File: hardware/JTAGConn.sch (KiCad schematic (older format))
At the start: 5 parts, among them CON1 FPC_6POS

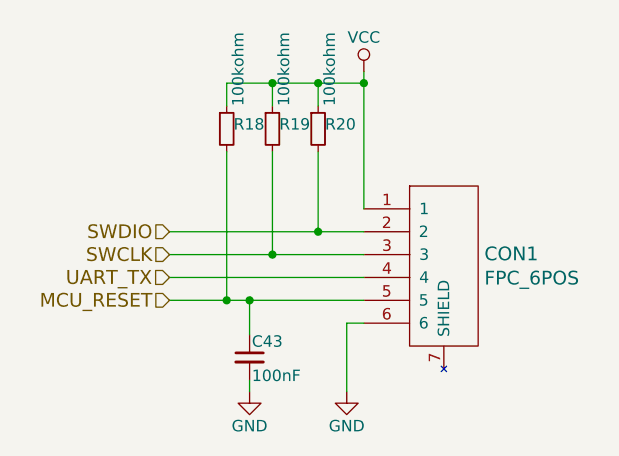
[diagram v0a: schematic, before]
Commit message: Finished work on Receiver RPi shield. Changed CLK to SI5351A. Minimized footprints for almost all Tayloe detector ICs. Added -12V to audio opamps. Prepared board for coexisting with Hifiberry.
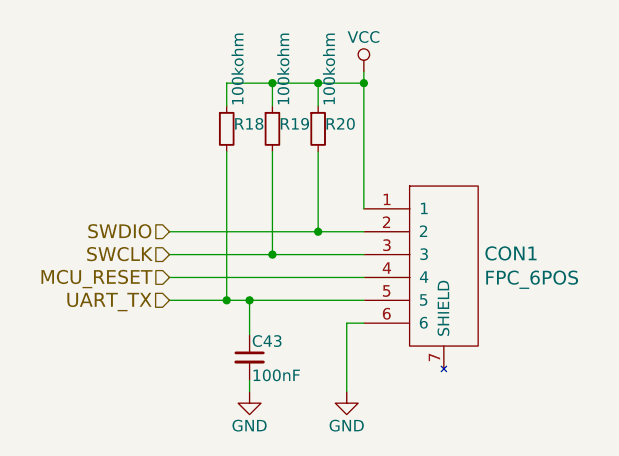
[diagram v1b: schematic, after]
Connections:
- net MCU_RESET: now also CON1.4; no longer C43.1, CON1.5, R18.2
- net UART_TX: now also C43.1, CON1.5, R18.2; no longer CON1.4
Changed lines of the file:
@@
 EESchema Schematic File Version 4
 LIBS:rf-receiver-cache
-EELAYER 26 0
+EELAYER 29 0
 EELAYER END
 $Descr A4 11693 8268
 encoding utf-8
-Sheet 5 7
+Sheet 5 6
 Title ""
 Date ""
@@
 Wire Wire Line
 	2900 3500 3350 3500
-Text HLabel 2900 3700 0    60   Input ~ 0
+Text HLabel 2900 3600 0    60   Input ~ 0
 MCU_RESET
 Text HLabel 2900 3500 0    60   Input ~ 0
@@
 U 1 1 5C507911
 P 4200 3800
+AR Path="/5C507911" Ref="CON1"  Part="1"
+AR Path="/58895F8E/5C507911" Ref="CON1"  Part="1"
 F 0 "CON1" H 4277 4103 60  0000 L CNN
 F 1 "FPC_6POS" H 4277 3997 60  0000 L CNN
@@
 Wire Wire Line
 	3750 2750 3750 3300
-Text HLabel 2900 3600 0    61   Input ~ 0
+Text HLabel 2900 3700 0    61   Input ~ 0
 UART_TX
 Wire Wire Line
